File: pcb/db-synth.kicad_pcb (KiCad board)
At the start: 2 copper layers, 42.8 x 40.8 mm, 29 parts, among them J1 JST XH 2P, J2 Conn_01x04, J3 JST XH 2P, J4 JST XH 2P, J5 JST XH 2P, U1 AVR128DB28, U2 MCP1702-3302E, U3 6N137

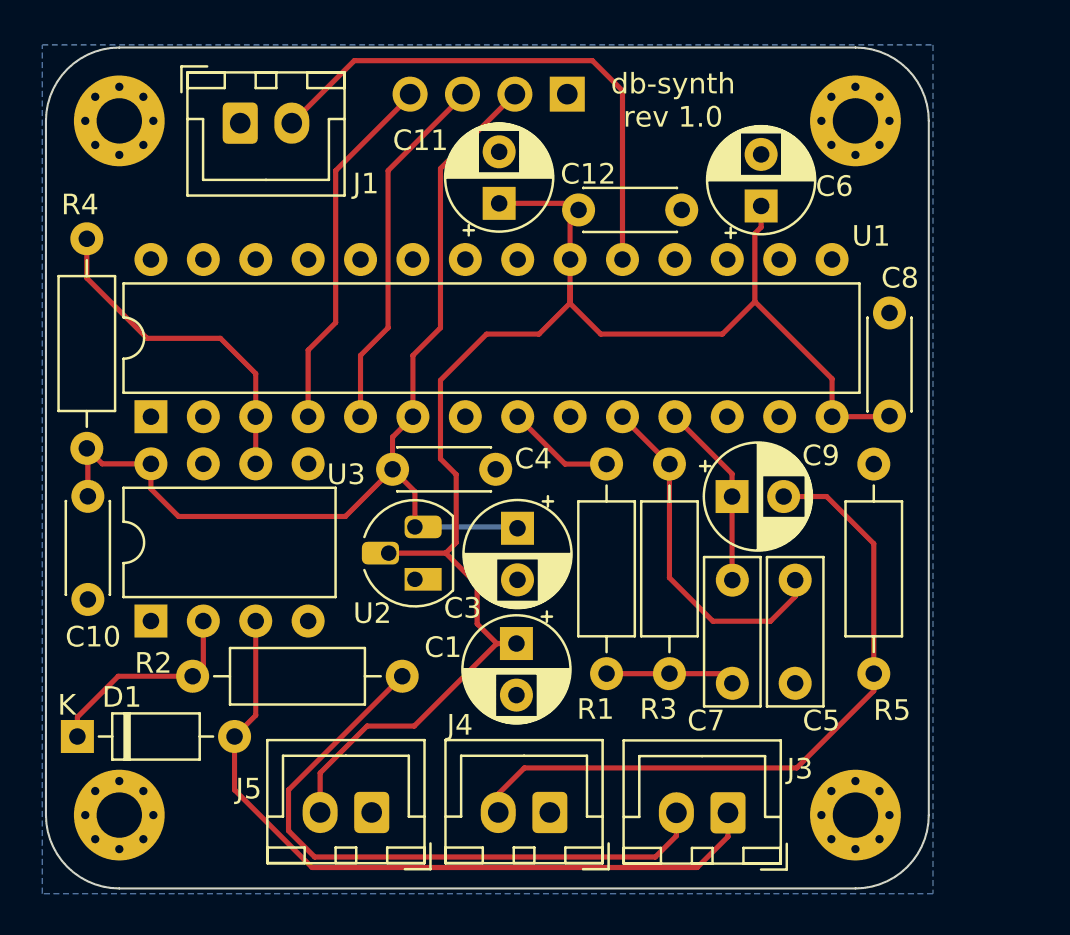
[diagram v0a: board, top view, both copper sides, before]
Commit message: pcb: new revision: 1.1
reduced part usage: no LDO and USART pull up resistor needed.
use default TWI pins, that are closer to connector, as MVIO is not
needed anymore.
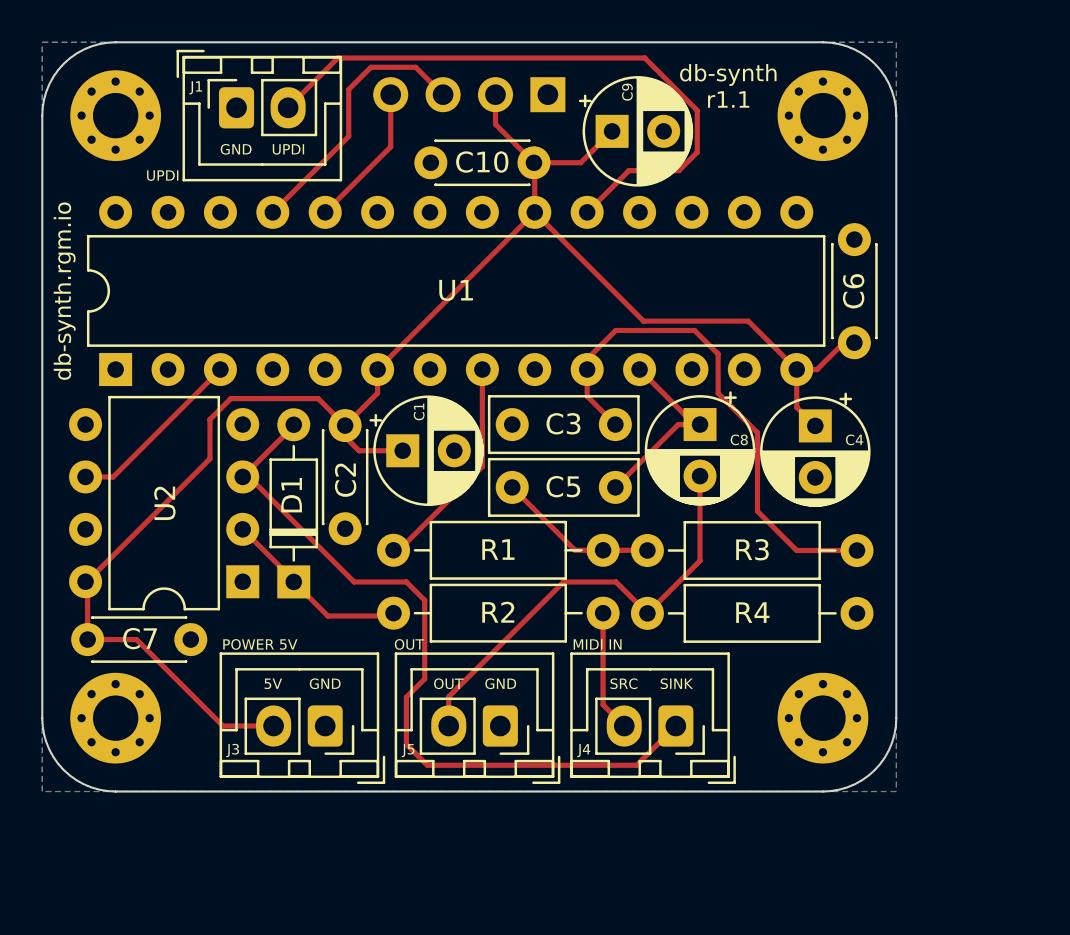
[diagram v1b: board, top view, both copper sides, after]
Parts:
- removed the C1 at (152.5, 108.5)
- removed the R4 at (131.7, 88.9)
- removed the U2 at (147.6, 105.4)
- H1, H2, H3, H4: value MountingHole -> MountingHole_Pad
- J1: footprint Connector_JST:JST_XH_B2B-XH-A_1x02_P2.50mm_Vertical -> Connector_JST_with_PinSocket:JST_XH_B2B-XH-A_PinSocket_1x02_P2.50mm_Vertical
- J2: value Conn_01x04 -> Pin Socket 1x4
- J3: renamed from J5; footprint Connector_JST:JST_XH_B2B-XH-A_1x02_P2.50mm_Vertical -> Connector_JST_with_PinSocket:JST_XH_B2B-XH-A_PinSocket_1x02_P2.50mm_Vertical
- J4: renamed from J3; footprint Connector_JST:JST_XH_B2B-XH-A_1x02_P2.50mm_Vertical -> Connector_JST_with_PinSocket:JST_XH_B2B-XH-A_PinSocket_1x02_P2.50mm_Vertical
- J5: renamed from J4; footprint Connector_JST:JST_XH_B2B-XH-A_1x02_P2.50mm_Vertical -> Connector_JST_with_PinSocket:JST_XH_B2B-XH-A_PinSocket_1x02_P2.50mm_Vertical
- moved H3 36.2 mm to (133.1, 112.1), turned to 0 degrees
- moved H2 34.1 mm to (167.4, 82.9), turned to 0 degrees
- moved H1 33.9 mm to (133.1, 82.9), turned to 0 degrees
- moved H4 29.0 mm to (167.4, 112.1), turned to 0 degrees
- moved C5 14.3 mm to (152.3, 101.0), turned to 0 degrees
- moved D1 12.9 mm to (141.7, 105.5), turned to 90 degrees
- moved C3 11.5 mm to (157.3, 97.9), turned to 180 degrees
- moved R1 11.1 mm to (146.6, 104.0), turned to 0 degrees
- moved C4 11.0 mm to (167.0, 98.0), turned to -90 degrees
- moved R2 10.2 mm to (146.6, 107.1)
- moved R4 7.28 mm to (169.0, 107.1), turned to 180 degrees
- moved C7 6.95 mm to (131.7, 108.3), turned to 0 degrees
- moved C1 6.71 mm to (147.0, 99.2), turned to 0 degrees
- moved C9 6.49 mm to (157.2, 83.7), turned to 0 degrees
- moved R3 6.06 mm to (158.9, 104.0), turned to 0 degrees
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- renumbered C3 to C1, C12 to C10, C4 to C2, C5 to C3, C6 to C4, C7 to C5, C8 to C6, C10 to C7, C9 to C8, C11 to C9, R5 to R4, U3 to U2
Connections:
- C1 pad 1: +3V3 -> VCC
- C2 pad 1: +3V3 -> VCC
- C7 pad 1: +3V3 -> VCC
- H1 pad 1: (no net) -> GND
- H2 pad 1: (no net) -> GND
- H3 pad 1: (no net) -> GND
- H4 pad 1: (no net) -> GND
- J2 pad 2: +3V3 -> VCC
- U1 pad 24: unconnected-(U1-Pad24) -> I2C_SDA
- U1 pad 25: unconnected-(U1-Pad25) -> I2C_SCL
- U1 pad 4: I2C_SDA -> unconnected-(U1-Pad4)
- U1 pad 5: I2C_SCL -> unconnected-(U1-Pad5)
- U1 pad 6: +3V3 -> VCC
- U2 pad 8: +3V3 -> VCC
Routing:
- net +3V3: track 49.1 -> 0.00 mm
- net Net-(J4-Pad2): track 30.6 -> 5.90 mm
- net Net-(C8-Pad2): track 33.6 -> 21.7 mm
- net I2C_SDA: track 17.7 -> 7.02 mm
- net OPAMP_INP: track 17.0 -> 25.4 mm
- net MIDI_RX: track 16.4 -> 8.70 mm
- net VCC: track 74.4 -> 81.9 mm
- net DAC_OUT: track 5.26 -> 10.7 mm
- net I2C_SCL: track 17.7 -> 13.1 mm
- net Net-(J1-Pad2): track 26.1 -> 30.5 mm
- net Net-(C5-Pad1): track 6.29 -> 7.82 mm
- net OPAMP_OUT: track 9.08 -> 10.4 mm
- net Net-(D1-Pad1): track 10.2 -> 9.15 mm
- net Net-(D1-Pad2): track 35.9 -> 36.5 mm
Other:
- board size 42.8 x 40.8 mm -> 41.4 x 36.3 mm
- board text added: "5V"
- board text added: "GND"
- board text added: "OUT"
- board text added: "SINK"
- board text added: "SRC"
- board text added: "UPDI"
- board text added: "db-synth r1.1"
- board text added: "db-synth.rgm.io"
- board text removed: "db-synth rev 1.0"

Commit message: pcb: new revision: 1.2
this revision adds a MIDI output, to allow daisy-chaining units to produce
richer sounds. it should work like a MIDI-thru, but I may want to not pass
messages processed by the current unit thru.
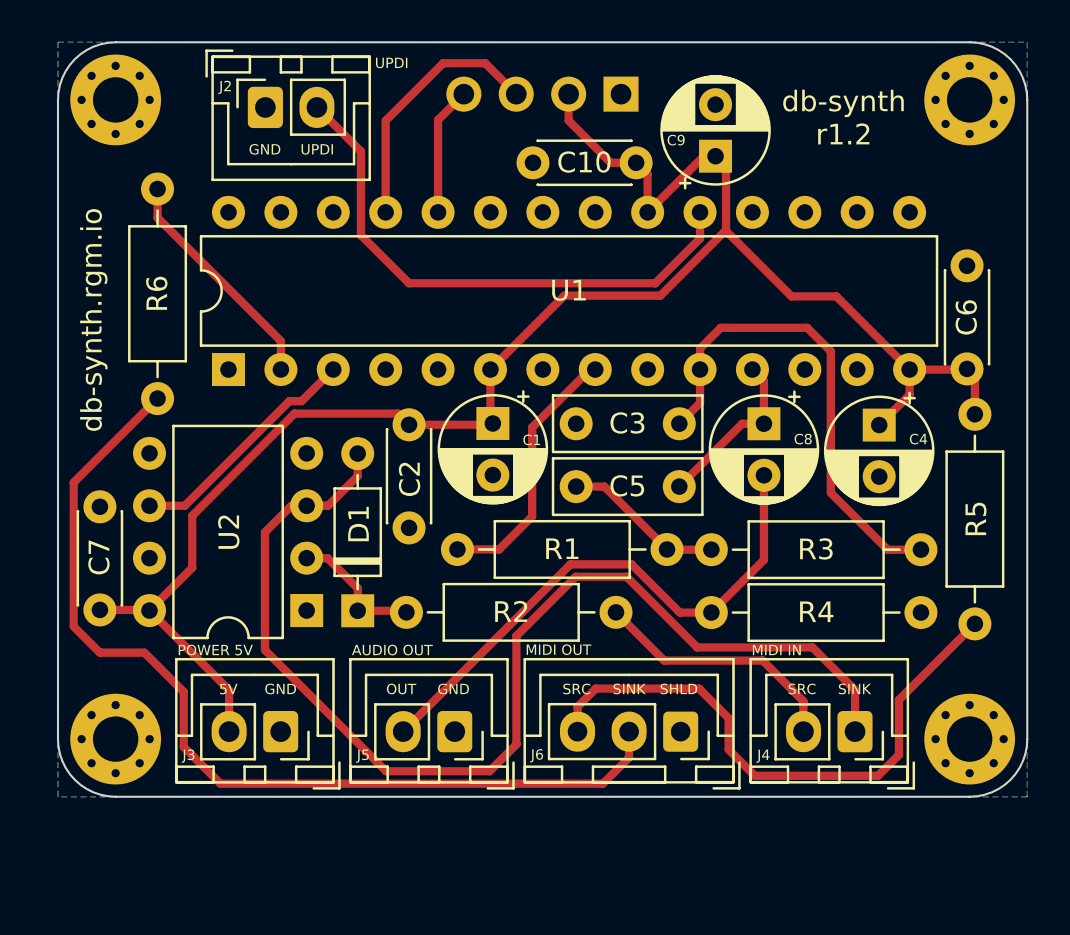
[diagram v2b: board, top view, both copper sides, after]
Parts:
- added J6: JST XH 3P, Connector_JST_with_PinSocket:JST_XH_B3B-XH-A_PinSocket_1x03_P2.50mm_Vertical, F.Cu at (160.5, 112.8)
- added R5: 220R, Resistor_THT:R_Axial_DIN0207_L6.3mm_D2.5mm_P10.16mm_Horizontal, F.Cu at (174.8, 107.6)
- added R6: 220R, Resistor_THT:R_Axial_DIN0207_L6.3mm_D2.5mm_P10.16mm_Horizontal, F.Cu at (135.1, 96.6)
- added REF**: OSHW-Logo_5.7x6mm_SilkScreen, Symbol:OSHW-Logo_5.7x6mm_SilkScreen, B.Cu at (167.1, 105.4)
- U1: value AVR128DB28 -> AVR128DB28 or AVR64DB28
- moved J4 8.69 mm to (168.9, 112.8)
- moved H4 7.18 mm to (174.5, 113.2)
- moved H2 7.15 mm to (174.5, 82.2)
- moved C6 5.61 mm to (174.4, 95.2)
- moved U1 5.47 mm to (138.6, 95.2)
- moved C9 5.16 mm to (162.2, 84.9), turned to 90 degrees
- moved C10 4.95 mm to (158.3, 85.2)
- moved C1 4.57 mm to (151.4, 97.9), turned to -90 degrees
- moved J1 3.55 mm to (157.6, 81.9)
- moved U2 3.40 mm to (142.4, 106.9)
- moved D1 3.40 mm to (144.8, 106.9)
- moved C4 3.10 mm to (170.1, 97.9)
- moved C8 3.10 mm to (164.5, 97.9)
- moved R1 3.10 mm to (149.7, 104.0)
- moved R3 3.10 mm to (162.0, 104.0)
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- renumbered J2 to J1, J1 to J2
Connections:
- U1 pad 2: unconnected-(U1-Pad2) -> MIDI_TX
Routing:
- net Net-(J6-Pad2): track 0.00 -> 46.2 mm
- net Net-(J6-Pad3): track 0.00 -> 28.1 mm
- net Net-(D1-Pad2): track 36.5 -> 55.8 mm
- net MIDI_TX: track 0.00 -> 11.2 mm
- net Net-(J4-Pad2): track 5.90 -> 12.3 mm
- net Net-(C8-Pad2): track 21.7 -> 27.0 mm
- net Net-(J2-Pad2): track 30.5 -> 26.7 mm
- net VCC: track 81.9 -> 85.5 mm
- net MIDI_RX: track 8.70 -> 11.6 mm
- net Net-(D1-Pad1): track 9.15 -> 6.56 mm
- net OPAMP_OUT: track 10.4 -> 8.22 mm
- net DAC_OUT: track 10.7 -> 12.8 mm
- net OPAMP_INP: track 25.4 -> 23.7 mm
- net I2C_SDA: track 7.02 -> 6.25 mm
- net I2C_SCL: track 13.1 -> 12.5 mm
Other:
- board size 41.4 x 36.3 mm -> 47 x 36.6 mm
- board text added: "db-synth r1.2"
- board text removed: "5V"
- board text removed: "GND"
- board text removed: "OUT"
- board text removed: "SINK"
- board text removed: "SRC"
- board text removed: "UPDI"
- board text removed: "db-synth r1.1"

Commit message: pcb: new revision: 1.3
this revision adds a 3rd pin to UPDI programming connector, to allow usage of
official Microchip probes, like PICKit 4, Atmel-ICE, etc.
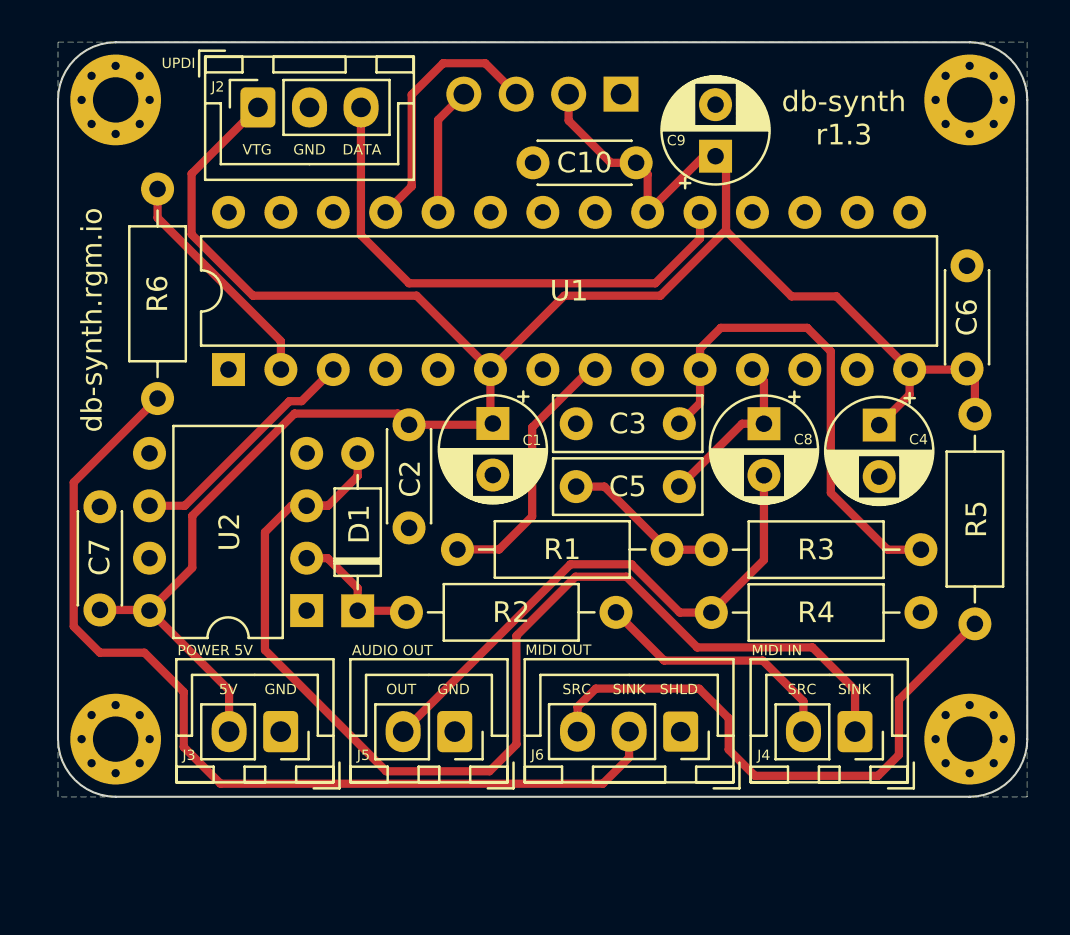
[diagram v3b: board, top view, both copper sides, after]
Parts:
- J2: value JST XH 2P -> JST XH 3P; footprint Connector_JST_with_PinSocket:JST_XH_B2B-XH-A_PinSocket_1x02_P2.50mm_Vertical -> Connector_JST_with_PinSocket:JST_XH_B3B-XH-A_PinSocket_1x03_P2.50mm_Vertical
- REF**: value OSHW-Logo_5.7x6mm_SilkScreen -> OSHW-Symbol_6.7x6mm_SilkScreen; footprint Symbol:OSHW-Logo_5.7x6mm_SilkScreen -> Symbol:OSHW-Symbol_6.7x6mm_SilkScreen
- moved J2 0.36 mm to (140.0, 82.5)
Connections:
- J2 pad 1: GND -> VCC
- J2 pad 2: Net-(J2-Pad2) -> GND
- U1 pad 19: Net-(J2-Pad2) -> Net-(J2-Pad3)
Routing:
- net Net-(J2-Pad2): track 26.7 -> 0.00 mm
- net Net-(J2-Pad3): track 0.00 -> 25.8 mm
- net VCC: track 85.5 -> 110.2 mm
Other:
- board text added: "db-synth r1.3"
- board text removed: "db-synth r1.2"
